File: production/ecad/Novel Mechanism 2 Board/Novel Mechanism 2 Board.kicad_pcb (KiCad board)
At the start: 2 copper layers, 37.4 x 45 mm, 19 parts, among them J1 1755736, J2 1755736, J3 0532611271, U1 L9958SBTR, U2 TMCS1108A4BQDRQ1

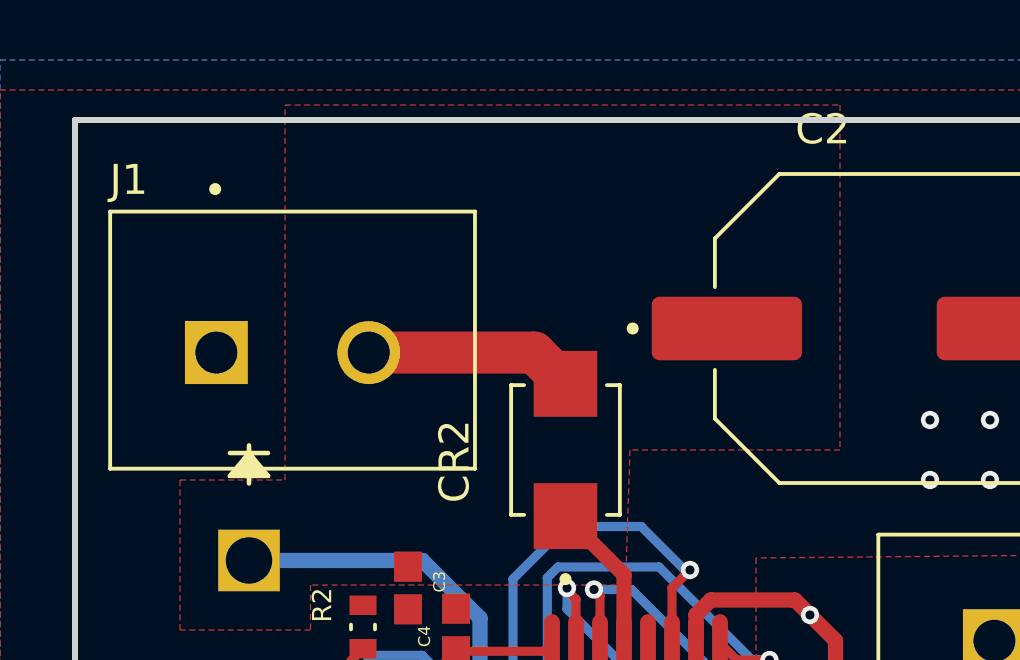
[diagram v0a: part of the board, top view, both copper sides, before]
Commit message: teardrops added
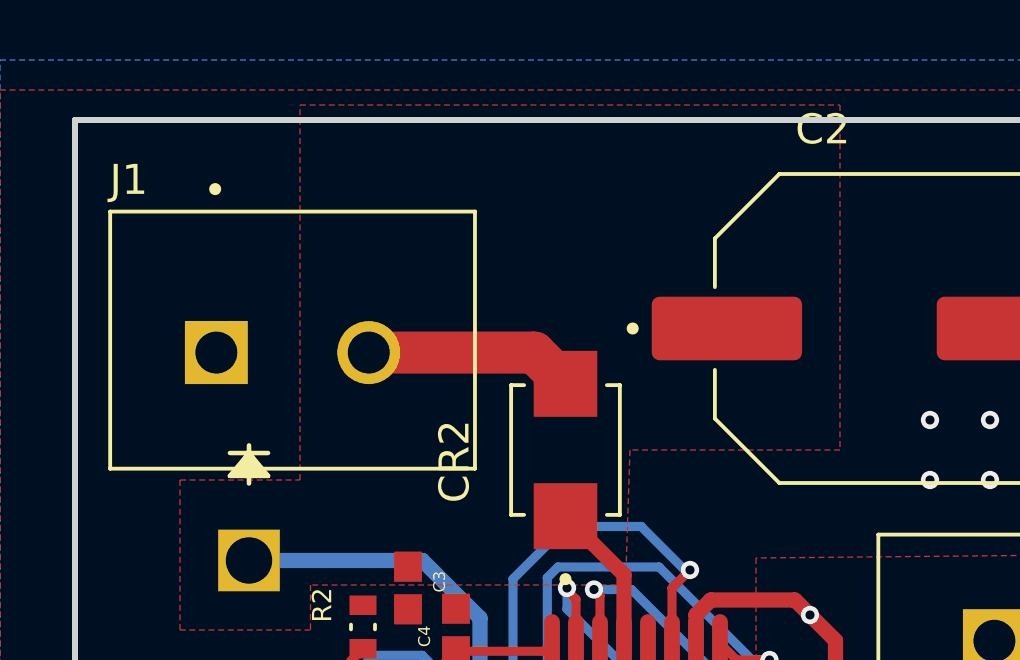
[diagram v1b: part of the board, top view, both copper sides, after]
